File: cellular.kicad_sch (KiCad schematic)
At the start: 44 parts, among them J6 USB_C_Receptacle_USB2.0_14P, J7 Conn_01x04_Pin, J8 SIM_Card_Shielded, J9 Conn_Coaxial, Q2 MMBT3904, Q3 MMBT3904, Q4 MMBT3904, SW4 SW_Push, U13 TPD3F303DPV, U14 SIM7080G

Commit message: schem: fix footprints
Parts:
- Q2, Q3, Q4: footprint Package_QFP:TQFP-44_10x10mm_P0.8mm -> Package_TO_SOT_SMD:SOT-23; symbol Device:Q_NPN -> Transistor_BJT:MMBT3904
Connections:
- net GND: now also Q2.2 (E), Q3.2 (E), Q4.2 (E); no longer Q2.E, Q3.E, Q4.E
- net at R37.2, R38.1: now also Q4.1 (B); no longer Q4.B
- net at C42.2, TP10.1, U14.39 (~{PWRKEY}): now also Q4.3 (C); no longer Q4.C
- net at R31.2, R32.1: now also Q2.1 (B); no longer Q2.B
- net at R34.2, R35.1: now also Q3.1 (B); no longer Q3.B
- net at D14.1 (K): now also Q3.3 (C); no longer Q3.C
- net at D13.1 (K): now also Q2.3 (C); no longer Q2.C
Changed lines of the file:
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@@
 	)
 	(symbol
-		(lib_id "Device:Q_NPN")
+		(lib_id "Transistor_BJT:MMBT3904")
 		(at 176.53 62.23 0)
 		(unit 1)
@@
 			)
 		)
-		(property "Footprint" "Package_QFP:TQFP-44_10x10mm_P0.8mm"
-			(at 181.61 59.69 0)
+		(property "Footprint" "Package_TO_SOT_SMD:SOT-23"
+			(at 181.61 64.135 0)
 			(hide yes)
 			(show_name no)
@@
 				(font
 					(size 1.27 1.27)
+					(italic yes)
 				)
+				(justify left)
 			)
 		)
-		(property "Datasheet" ""
+		(property "Datasheet" "https://www.onsemi.com/pdf/datasheet/pzt3904-d.pdf"
 			(at 176.53 62.23 0)
 			(hide yes)
@@
 					(size 1.27 1.27)
 				)
+				(justify left)
 			)
 		)
-		(property "Description" "NPN bipolar junction transistor"
+		(property "Description" "0.2A Ic, 40V Vce, Small Signal NPN Transistor, SOT-23"
 			(at 176.53 62.23 0)
 			(hide yes)
@@
 			)
 		)
-		(pin "C"
+		(property "Sim.Device" "NPN"
+			(at 176.53 62.23 0)
+			(hide yes)
+			(show_name no)
+			(do_not_autoplace no)
+			(effects
+				(font
+					(size 1.27 1.27)
+				)
+			)
 		)
-		(pin "E"
+		(property "Sim.Pins" "1=B 2=E 3=C"
+			(at 176.53 62.23 0)
+			(hide yes)
+			(show_name no)
+			(do_not_autoplace no)
+			(effects
+				(font
+					(size 1.27 1.27)
+				)
+			)
+		)
+		(pin "3"
+		)
+		(pin "1"
 		)
-		(pin "B"
+		(pin "2"
 		)
 		(instances
@@
 	)
 	(symbol
-		(lib_id "Device:Q_NPN")
+		(lib_id "Transistor_BJT:MMBT3904")
 		(at 127 50.8 0)
 		(unit 1)
@@
 			)
 		)
-		(property "Footprint" "Package_QFP:TQFP-44_10x10mm_P0.8mm"
-			(at 132.08 48.26 0)
+		(property "Footprint" "Package_TO_SOT_SMD:SOT-23"
+			(at 132.08 52.705 0)
 			(hide yes)
 			(show_name no)
@@
 				(font
 					(size 1.27 1.27)
+					(italic yes)
 				)
+				(justify left)
 			)
 		)
-		(property "Datasheet" ""
+		(property "Datasheet" "https://www.onsemi.com/pdf/datasheet/pzt3904-d.pdf"
 			(at 127 50.8 0)
 			(hide yes)
@@
 					(size 1.27 1.27)
 				)
+				(justify left)
 			)
 		)
-		(property "Description" "NPN bipolar junction transistor"
+		(property "Description" "0.2A Ic, 40V Vce, Small Signal NPN Transistor, SOT-23"
 			(at 127 50.8 0)
 			(hide yes)
@@
 			)
 		)
-		(pin "C"
+		(property "Sim.Device" "NPN"
+			(at 127 50.8 0)
+			(hide yes)
+			(show_name no)
+			(do_not_autoplace no)
+			(effects
+				(font
+					(size 1.27 1.27)
+				)
+			)
+		)
+		(property "Sim.Pins" "1=B 2=E 3=C"
+			(at 127 50.8 0)
+			(hide yes)
+			(show_name no)
+			(do_not_autoplace no)
+			(effects
+				(font
+					(size 1.27 1.27)
+				)
+			)
+		)
+		(pin "3"
 		)
-		(pin "E"
+		(pin "2"
 		)
-		(pin "B"
+		(pin "1"
 		)
 		(instances
@@
 	)
 	(symbol
-		(lib_id "Device:Q_NPN")
+		(lib_id "Transistor_BJT:MMBT3904")
 		(at 88.9 50.8 0)
 		(unit 1)
@@
 			)
 		)
-		(property "Footprint" "Package_QFP:TQFP-44_10x10mm_P0.8mm"
-			(at 93.98 48.26 0)
+		(property "Footprint" "Package_TO_SOT_SMD:SOT-23"
+			(at 93.98 52.705 0)
 			(hide yes)
 			(show_name no)
@@
 				(font
 					(size 1.27 1.27)
+					(italic yes)
 				)
+				(justify left)
 			)
 		)
-		(property "Datasheet" ""
+		(property "Datasheet" "https://www.onsemi.com/pdf/datasheet/pzt3904-d.pdf"
 			(at 88.9 50.8 0)
 			(hide yes)
@@
 					(size 1.27 1.27)
 				)
+				(justify left)
 			)
 		)
-		(property "Description" "NPN bipolar junction transistor"
+		(property "Description" "0.2A Ic, 40V Vce, Small Signal NPN Transistor, SOT-23"
 			(at 88.9 50.8 0)
 			(hide yes)
@@
 			)
 		)
-		(pin "C"
+		(property "Sim.Device" "NPN"
+			(at 88.9 50.8 0)
+			(hide yes)
+			(show_name no)
+			(do_not_autoplace no)
+			(effects
+				(font
+					(size 1.27 1.27)
+				)
+			)
 		)
-		(pin "E"
+		(property "Sim.Pins" "1=B 2=E 3=C"
+			(at 88.9 50.8 0)
+			(hide yes)
+			(show_name no)
+			(do_not_autoplace no)
+			(effects
+				(font
+					(size 1.27 1.27)
+				)
+			)
 		)
-		(pin "B"
+		(pin "2"
+		)
+		(pin "3"
+		)
+		(pin "1"
 		)
 		(instances

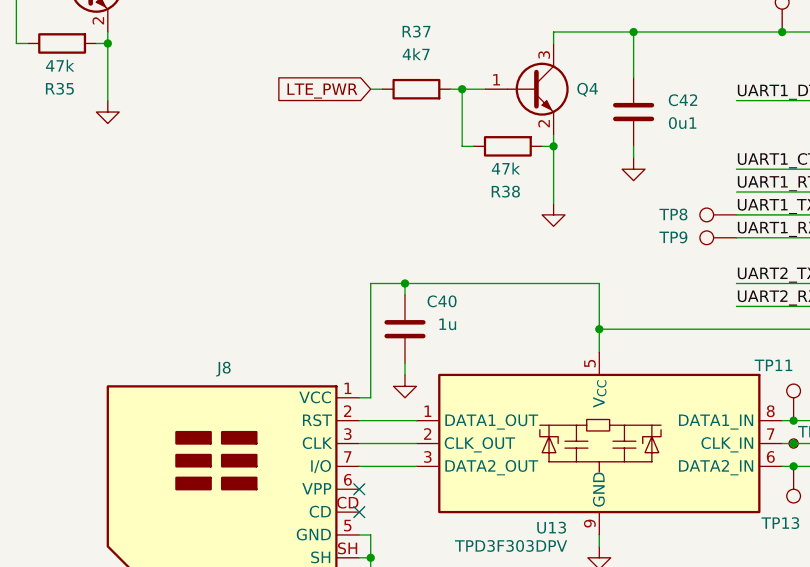
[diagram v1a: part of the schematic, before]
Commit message: schem: update gnd net class priority
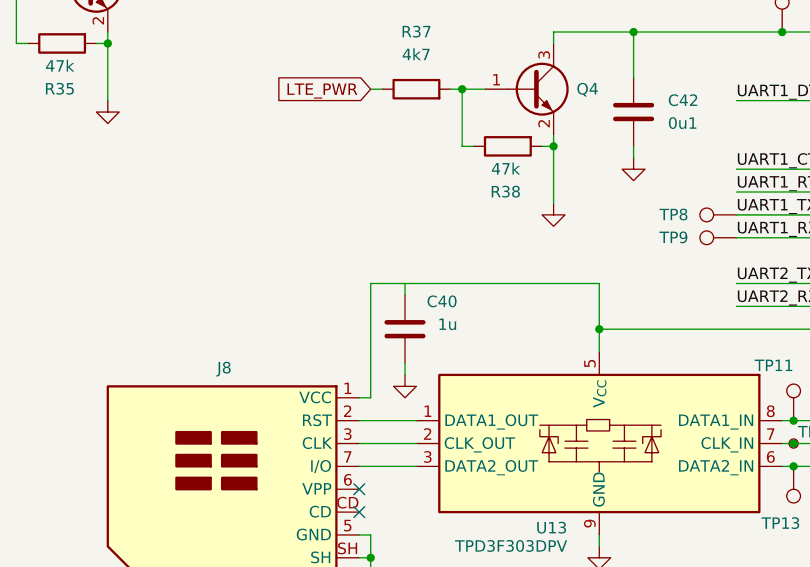
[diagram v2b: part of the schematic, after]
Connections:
- net at J8.1 (VCC), U13.5 (V_{CC}), U14.18 (SIM_VDD): no longer C40.2
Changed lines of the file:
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@@
-	)
-	(junction
-		(at 162.56 83.82)
-		(diameter 0)
-		(color 0 0 0 0)
 	)
 	(junction

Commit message: schem: update 10u caps to 0603
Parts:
- C46, C47, C48, C49, C50: footprint Capacitor_SMD:C_0402_1005Metric -> Capacitor_SMD:C_0603_1608Metric; JLCPCB Part # C15525 -> C19702; Manufacturer Part Number CL05A106MQ5NUNC -> CL10A106KP8NNNC
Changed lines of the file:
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@@
 			)
 		)
-		(property "Footprint" "Capacitor_SMD:C_0402_1005Metric"
+		(property "Footprint" "Capacitor_SMD:C_0603_1608Metric"
 			(at 249.2248 33.02 0)
 			(hide yes)
@@
 			)
 		)
-		(property "JLCPCB Part #" "C15525"
+		(property "JLCPCB Part #" "C19702"
 			(at 250.19 29.21 0)
 			(hide yes)
@@
 			)
 		)
-		(property "Manufacturer Part Number" "CL05A106MQ5NUNC"
+		(property "Manufacturer Part Number" "CL10A106KP8NNNC"
 			(at 250.19 29.21 0)
 			(hide yes)
@@
 			)
 		)
-		(property "Footprint" "Capacitor_SMD:C_0402_1005Metric"
+		(property "Footprint" "Capacitor_SMD:C_0603_1608Metric"
 			(at 259.3848 33.02 0)
 			(hide yes)
@@
 			)
 		)
-		(property "JLCPCB Part #" "C15525"
+		(property "JLCPCB Part #" "C19702"
 			(at 260.35 29.21 0)
 			(hide yes)
@@
 			)
 		)
-		(property "Manufacturer Part Number" "CL05A106MQ5NUNC"
+		(property "Manufacturer Part Number" "CL10A106KP8NNNC"
 			(at 260.35 29.21 0)
 			(hide yes)
@@
 			)
 		)
-		(property "Footprint" "Capacitor_SMD:C_0402_1005Metric"
+		(property "Footprint" "Capacitor_SMD:C_0603_1608Metric"
 			(at 254.3048 33.02 0)
 			(hide yes)
@@
 			)
 		)
-		(property "JLCPCB Part #" "C15525"
+		(property "JLCPCB Part #" "C19702"
 			(at 255.27 29.21 0)
 			(hide yes)
@@
 			)
 		)
-		(property "Manufacturer Part Number" "CL05A106MQ5NUNC"
+		(property "Manufacturer Part Number" "CL10A106KP8NNNC"
 			(at 255.27 29.21 0)
 			(hide yes)
@@
 			)
 		)
-		(property "Footprint" "Capacitor_SMD:C_0402_1005Metric"
+		(property "Footprint" "Capacitor_SMD:C_0603_1608Metric"
 			(at 264.4648 33.02 0)
 			(hide yes)
@@
 			)
 		)
-		(property "JLCPCB Part #" "C15525"
+		(property "JLCPCB Part #" "C19702"
 			(at 265.43 29.21 0)
 			(hide yes)
@@
 			)
 		)
-		(property "Manufacturer Part Number" "CL05A106MQ5NUNC"
+		(property "Manufacturer Part Number" "CL10A106KP8NNNC"
 			(at 265.43 29.21 0)
 			(hide yes)
@@
 			)
 		)
-		(property "Footprint" "Capacitor_SMD:C_0402_1005Metric"
+		(property "Footprint" "Capacitor_SMD:C_0603_1608Metric"
 			(at 244.1448 33.02 0)
 			(hide yes)
@@
 			)
 		)
-		(property "JLCPCB Part #" "C15525"
+		(property "JLCPCB Part #" "C19702"
 			(at 245.11 29.21 0)
 			(hide yes)
@@
 			)
 		)
-		(property "Manufacturer Part Number" "CL05A106MQ5NUNC"
+		(property "Manufacturer Part Number" "CL10A106KP8NNNC"
 			(at 245.11 29.21 0)
 			(hide yes)

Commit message: pcb: add sim layout
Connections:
- net at TP12.1, U14.16 (SIM_CLK): now also U13.2 (CLK_OUT); no longer U13.7 (CLK_IN)
- net at J8.1 (VCC), U13.5 (V_{CC}), U14.18 (SIM_VDD): now also C40.2
- net at U13.1 (DATA1_OUT): now also TP11.1, U14.15 (SIM_DATA); no longer J8.2 (RST)
- net at J8.3 (CLK): now also U13.7 (CLK_IN); no longer U13.2 (CLK_OUT)
- net at U13.3 (DATA2_OUT): now also TP13.1, U14.17 (SIM_RST); no longer J8.7 (I/O)
- new net: J8.2 (RST), U13.6 (DATA2_IN)
- new net: J8.7 (I/O), U13.8 (DATA1_IN)
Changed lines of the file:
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@@
 	)
 	(junction
+		(at 162.56 83.82)
+		(diameter 0)
+		(color 0 0 0 0)
+	)
+	(junction
 		(at 55.88 158.75)
 		(diameter 0)
@@
 	(wire
 		(pts
-			(xy 41.91 102.87) (xy 41.91 101.6)
+			(xy 162.56 83.82) (xy 184.15 83.82)
 		)
 		(stroke
@@
 	(wire
 		(pts
-			(xy 208.28 88.9) (xy 184.15 88.9)
+			(xy 41.91 102.87) (xy 41.91 101.6)
 		)
 		(stroke
@@
 	(wire
 		(pts
-			(xy 205.74 101.6) (xy 204.47 101.6)
+			(xy 208.28 88.9) (xy 184.15 88.9)
 		)
 		(stroke
@@
 	(wire
 		(pts
-			(xy 52.07 182.88) (xy 52.07 186.69)
+			(xy 205.74 101.6) (xy 204.47 101.6)
 		)
 		(stroke
@@
 	(wire
 		(pts
-			(xy 265.43 24.13) (xy 269.24 24.13)
+			(xy 52.07 182.88) (xy 52.07 186.69)
 		)
 		(stroke
@@
 	(wire
 		(pts
-			(xy 162.56 83.82) (xy 162.56 85.09)
+			(xy 265.43 24.13) (xy 269.24 24.13)
 		)
 		(stroke
@@
 	(wire
 		(pts
-			(xy 158.75 83.82) (xy 184.15 83.82)
+			(xy 158.75 83.82) (xy 162.56 83.82)
 		)
 		(stroke
@@
 	(wire
 		(pts
+			(xy 162.56 83.82) (xy 162.56 85.09)
+		)
+		(stroke
+			(width 0)
+			(type default)
+		)
+	)
+	(wire
+		(pts
 			(xy 36.83 101.6) (xy 36.83 125.73)
 		)
@@
 		(lib_id "Power_Protection:TPD3F303DPV")
 		(at 184.15 101.6 0)
-		(mirror y)
 		(unit 1)
 		(body_style 1)
@@
 		(dnp no)
 		(property "Reference" "U13"
-			(at 180.594 110.998 0)
+			(at 167.386 111.76 0)
 			(show_name no)
 			(do_not_autoplace no)
@@
 		)
 		(property "Value" "TPD3F303DPV"
-			(at 180.594 113.03 0)
+			(at 167.386 113.792 0)
 			(show_name no)
 			(do_not_autoplace no)
@@
 		)
 		(property "Footprint" "Package_SON:Texas_R-PUSON-N8_USON-8-1EP_1.6x2.1mm_P0.5mm_EP0.4x1.7mm"
-			(at 185.42 111.76 0)
+			(at 182.88 111.76 0)
 			(hide yes)
 			(show_name no)
@@
 		)
 		(property "Datasheet" "https://www.ti.com/lit/gpn/tpd3f303"
-			(at 180.34 114.3 0)
+			(at 187.96 114.3 0)
 			(hide yes)
 			(show_name no)

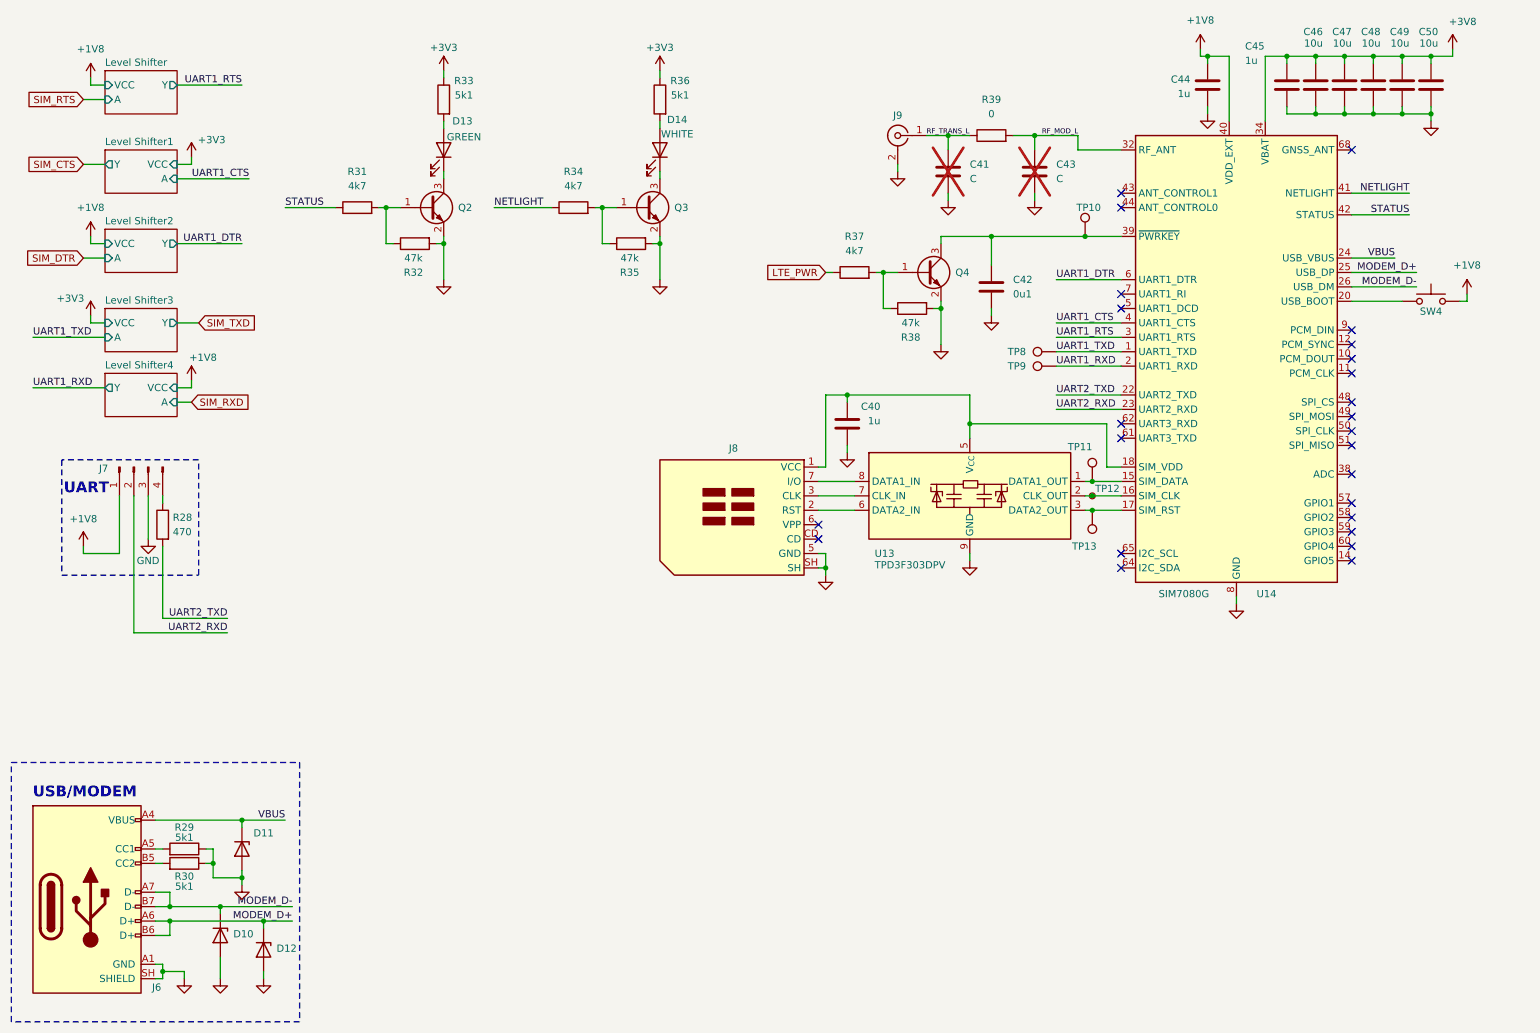
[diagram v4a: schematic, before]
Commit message: pcb: add placement
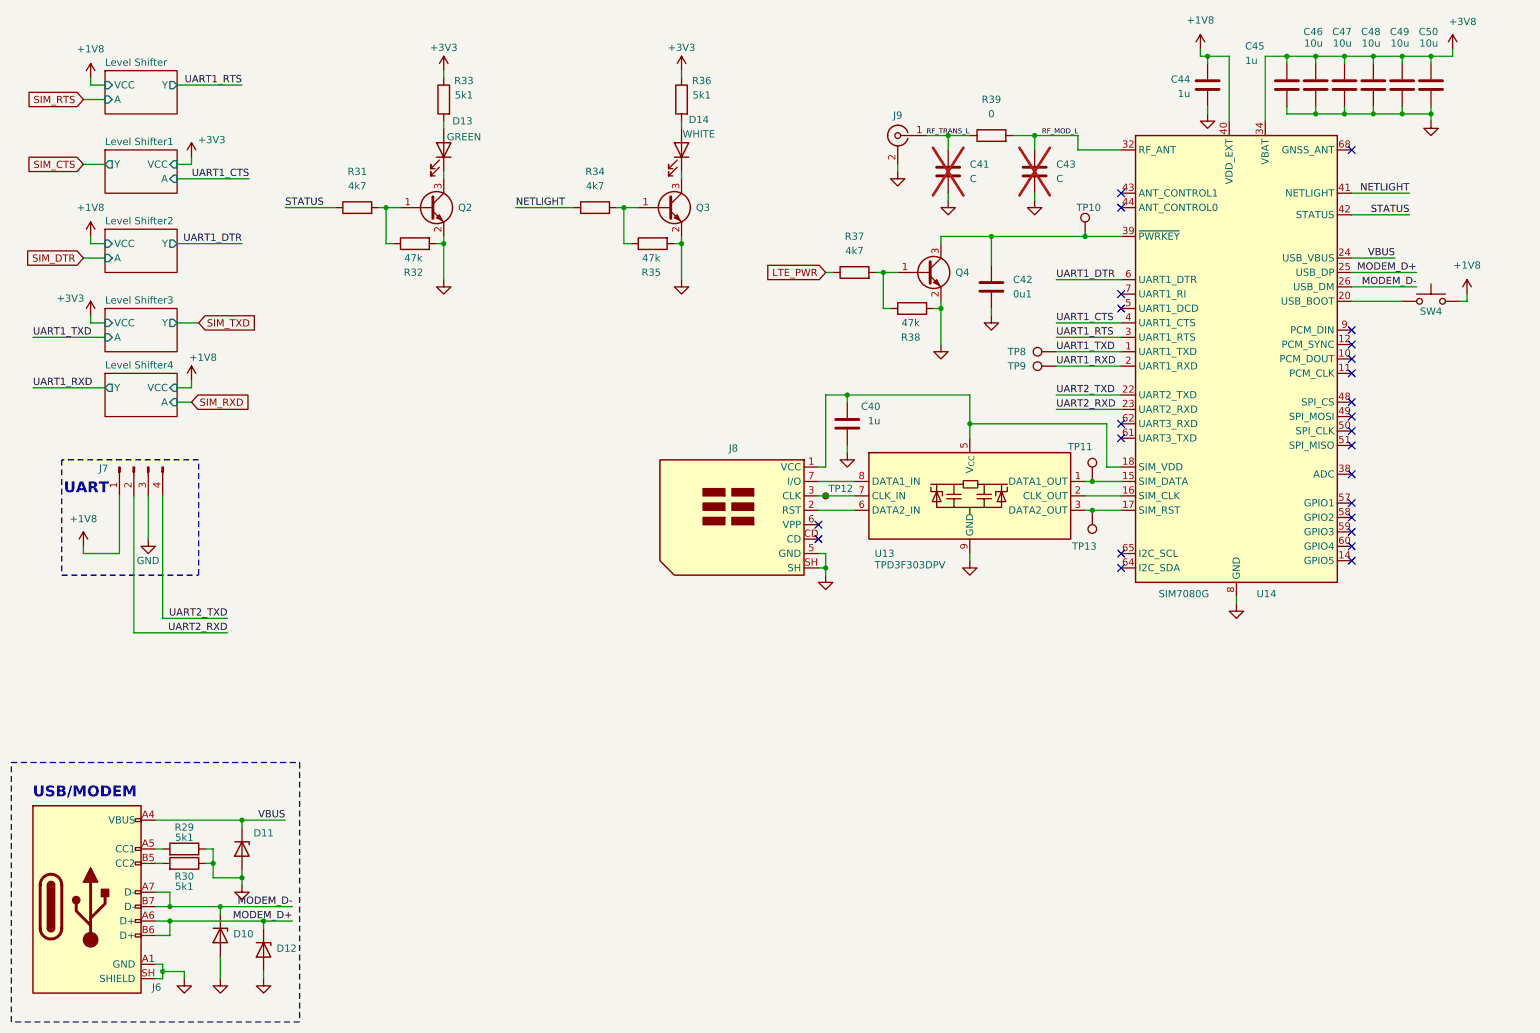
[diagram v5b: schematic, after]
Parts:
- removed R28: 470, Resistor_SMD:R_0402_1005Metric, symbol Device:R
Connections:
- net UART2_TXD: now also J7.4 (Pin_4)
- net at U13.2 (CLK_OUT), U14.16 (SIM_CLK): no longer TP12.1
- net at J8.3 (CLK), U13.7 (CLK_IN): now also TP12.1
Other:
- moved on the sheet: D14, Q3, R34, R35, R36

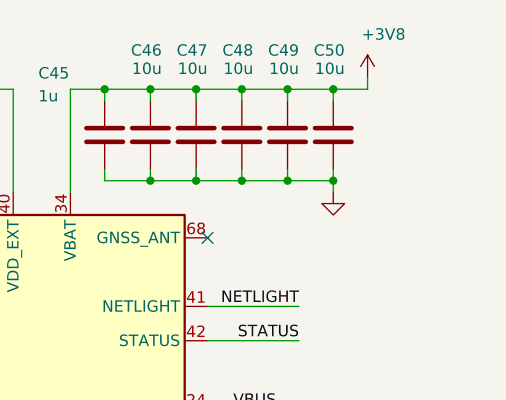
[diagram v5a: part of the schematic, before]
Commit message: schem: add 2 bulk cap to modem +3v8
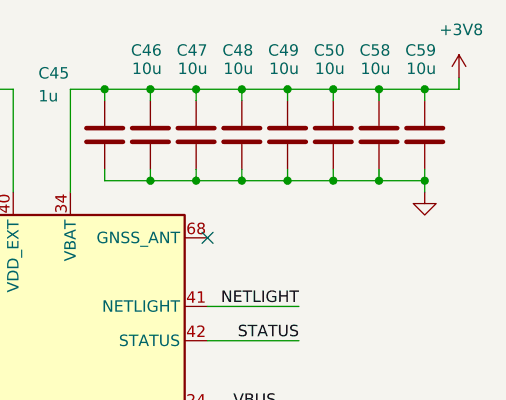
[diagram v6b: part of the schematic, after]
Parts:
- added C58, C59: 10u, Capacitor_SMD:C_0603_1608Metric, symbol Device:C
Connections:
- net +3V8: now also C58.1, C59.1
- net GND: now also C58.2, C59.2
